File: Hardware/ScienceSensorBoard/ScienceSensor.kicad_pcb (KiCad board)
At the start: 2 copper layers, 96.5 x 94.5 mm, 94 parts, among them J1 Conn_02x03_Counter_Clockwise, J2 RJ45_LED_Shielded, Q1 SI4156DY, Q10 BSS138, Q11 SI4156DY, Q2 SI4156DY, Q3 SI4156DY, Q4 BSS138, Q5 BSS138, Q6 BSS138, Q7 BSS138, Q8 BSS138, Q9 BSS138, U1 TSR_1-2450, U2 OKI-78SR-3.3_1.5-W36H-C, U3 Teensy4.1_DEV-16771, U6 IRS2005S, U7 IRS2005S

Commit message: Layout Reviews Changes
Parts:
- moved V1 0.51 mm to (100.6, 50.8)
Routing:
- net +12V: track 120.9 -> 126.5 mm
- net Micro_FWD: track 63.6 -> 67.0 mm
- net Micro_RVS: track 60.5 -> 63.7 mm
- net +3V3: track 190.7 -> 192.2 mm
- net LED_315: track 49.6 -> 48.2 mm
- net +5V: track 196.6 -> 197.5 mm
- net GND: vias 24 -> 32

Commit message: Molex_SL_06
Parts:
- removed G***: LOGO, MRDT_Silkscreens:0_MRDT_Logo_7.5mm
- Conn4: value Molex_SL_07 -> Molex_SL_06; footprint MRDT_Connectors:MOLEX_SL_07_Horizontal -> UVLEDs:705550040
- moved Conn4 2.54 mm to (108.0, 105.9), turned to -90 degrees
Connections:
- Conn4 pad 4: LED_260 -> LED_275
- Conn4 pad 5: LED_275 -> LED_280
- Conn4 pad 6: LED_280 -> LED_315
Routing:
- net +12V: track 126.5 -> 129.8 mm

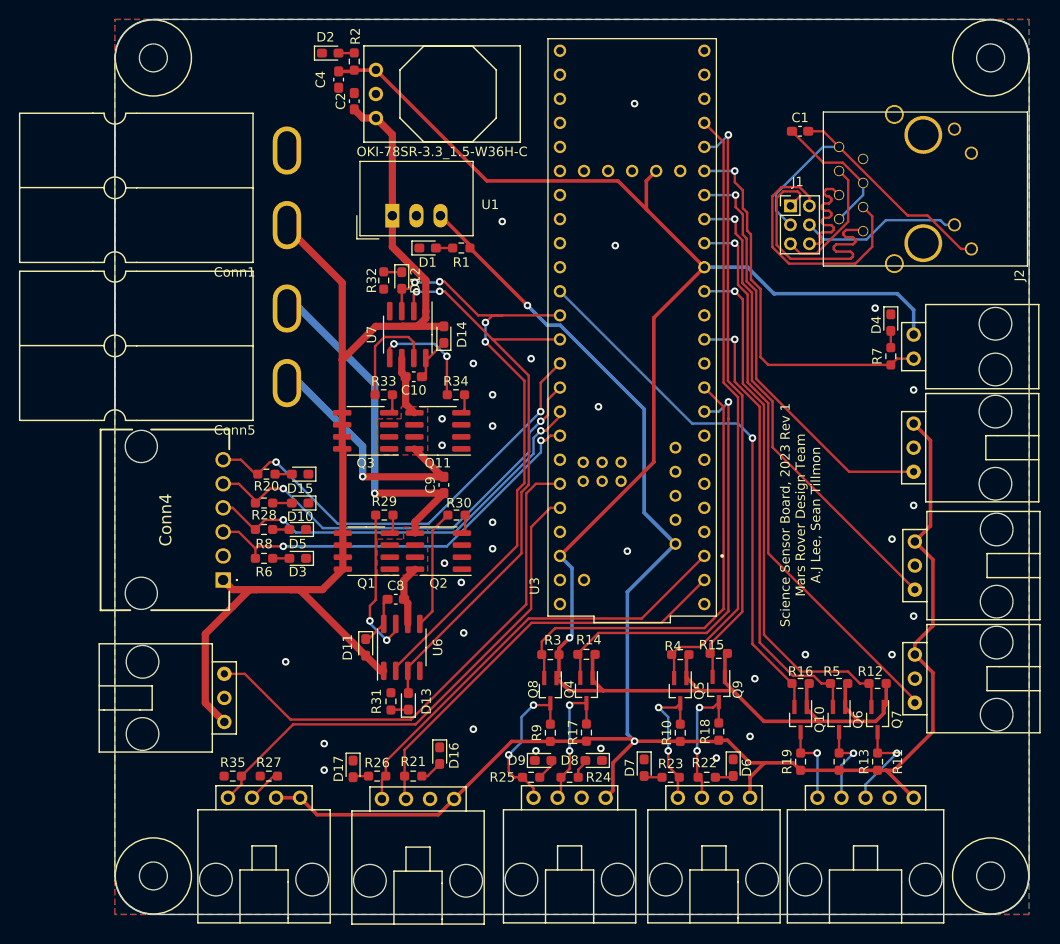
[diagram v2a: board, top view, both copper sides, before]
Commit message: Fixed Schematic error, Labeled some LEDs
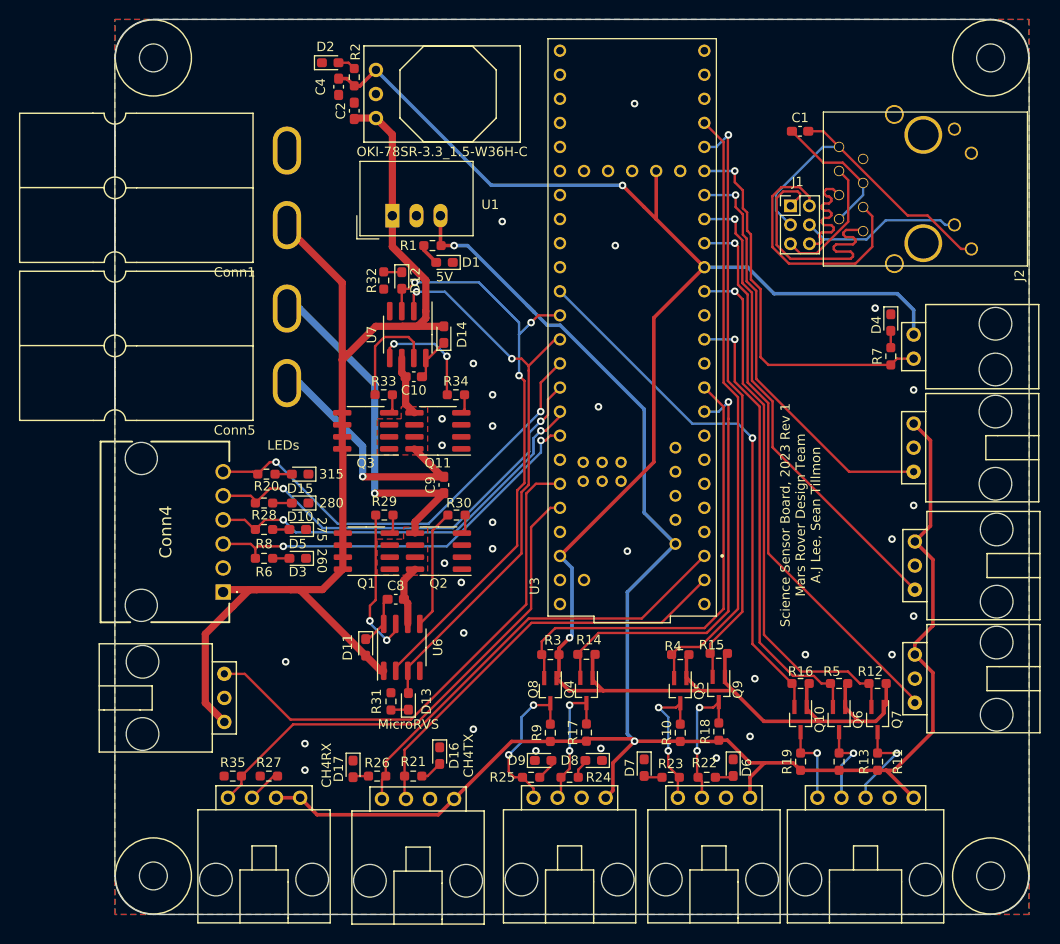
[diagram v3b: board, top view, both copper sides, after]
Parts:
- moved R1 3.06 mm to (130.0, 70.6)
- moved D1 2.34 mm to (131.3, 72.4), turned to 180 degrees
- moved R2 1.65 mm to (121.8, 52.8)
- moved Conn4 1.27 mm to (108.0, 107.2)
- moved C2 1.02 mm to (121.8, 56.4)
- moved D2 1.02 mm to (119.3, 51.3)
- moved C4 0.76 mm to (120.1, 53.8)
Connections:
- Conn4 pad 3: unconnected-(Conn4-Pad3) -> LED_260
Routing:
- net +5V: track 197.5 -> 200.2 mm
- net Micro_FWD: track 67.0 -> 64.6 mm, vias 4 -> 3
- net Micro_RVS: track 63.7 -> 61.6 mm
- net +3V3: track 192.2 -> 193.5 mm, vias 1 -> 2
- net +12V: track 129.8 -> 129.1 mm
- net Net-(D1-Pad2): track 1.77 -> 2.32 mm
- net LED_280: track 47.2 -> 46.7 mm
- net LED_260: track 43.0 -> 42.5 mm
- net LED_315: track 48.2 -> 47.7 mm
- net LED_275: track 44.0 -> 43.5 mm
- net GND: vias 32 -> 31
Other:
- board text added: "260"
- board text added: "275"
- board text added: "280"
- board text added: "315"
- board text added: "5V"
- board text added: "CH4RX"
- board text added: "CH4TX"
- board text added: "MicroRVS"

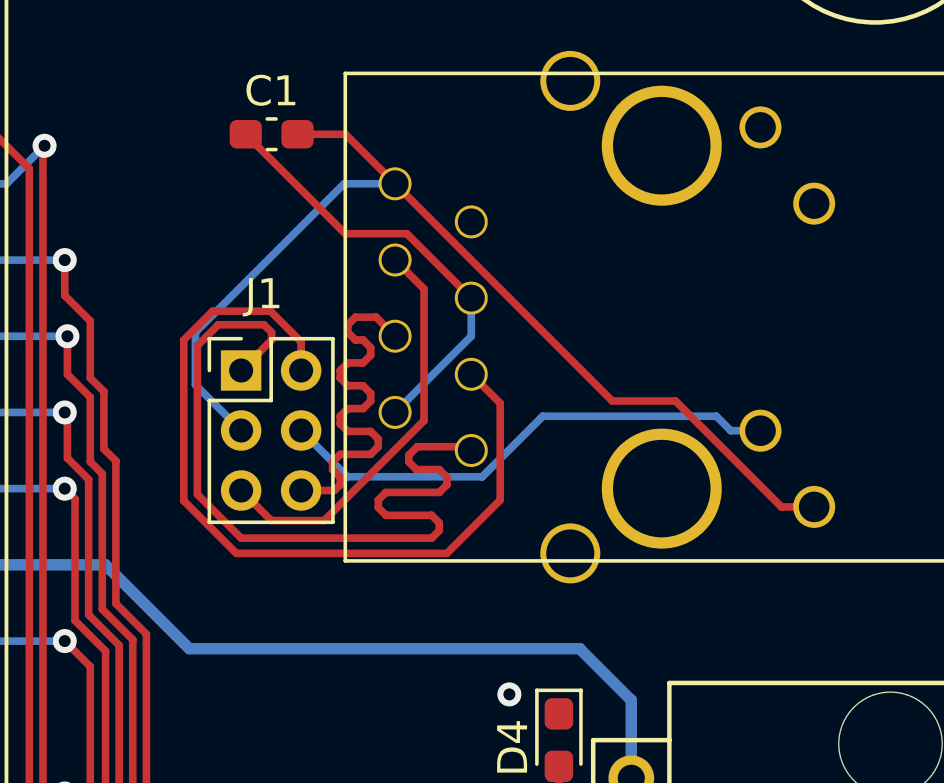
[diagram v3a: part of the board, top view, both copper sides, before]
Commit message: Flipped 2x3, updated sheet boms
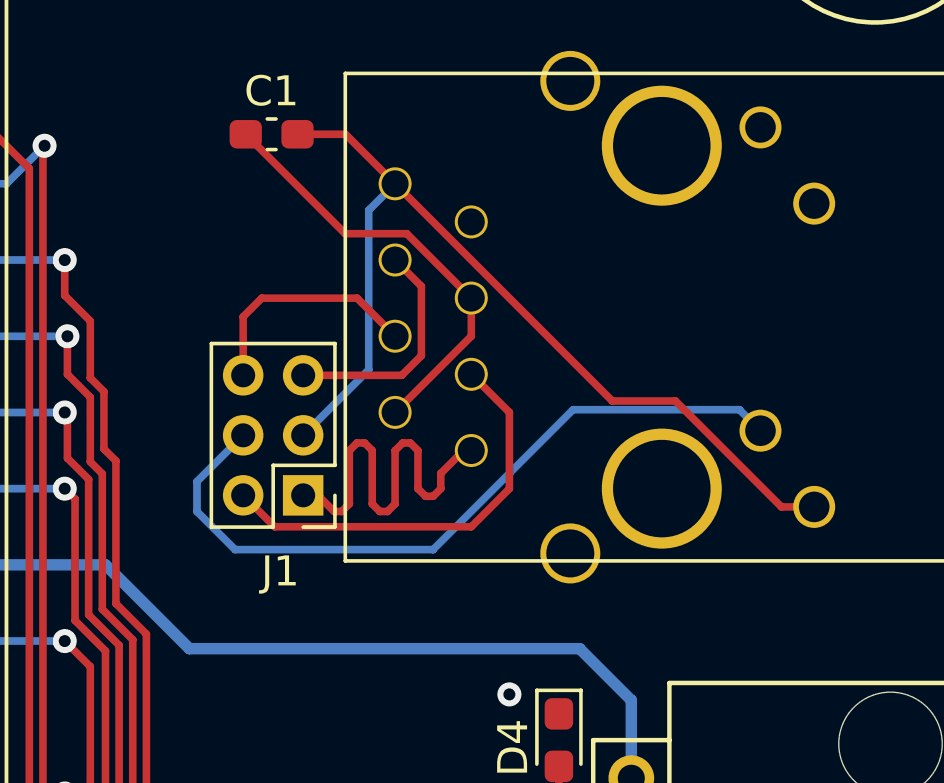
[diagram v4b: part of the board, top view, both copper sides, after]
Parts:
- moved J1 4.65 mm to (169.9, 70.6), turned to 180 degrees
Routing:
- net /Tx+: track 27.7 -> 14.2 mm
- net /Tx-: track 27.6 -> 14.2 mm
- net Net-(J1-Pad4): track 17.0 -> 24.7 mm
- net /Rx-: track 13.6 -> 7.76 mm
- net /Rx+: track 13.6 -> 7.80 mm
- net Net-(C1-Pad2): track 35.0 -> 32.0 mm

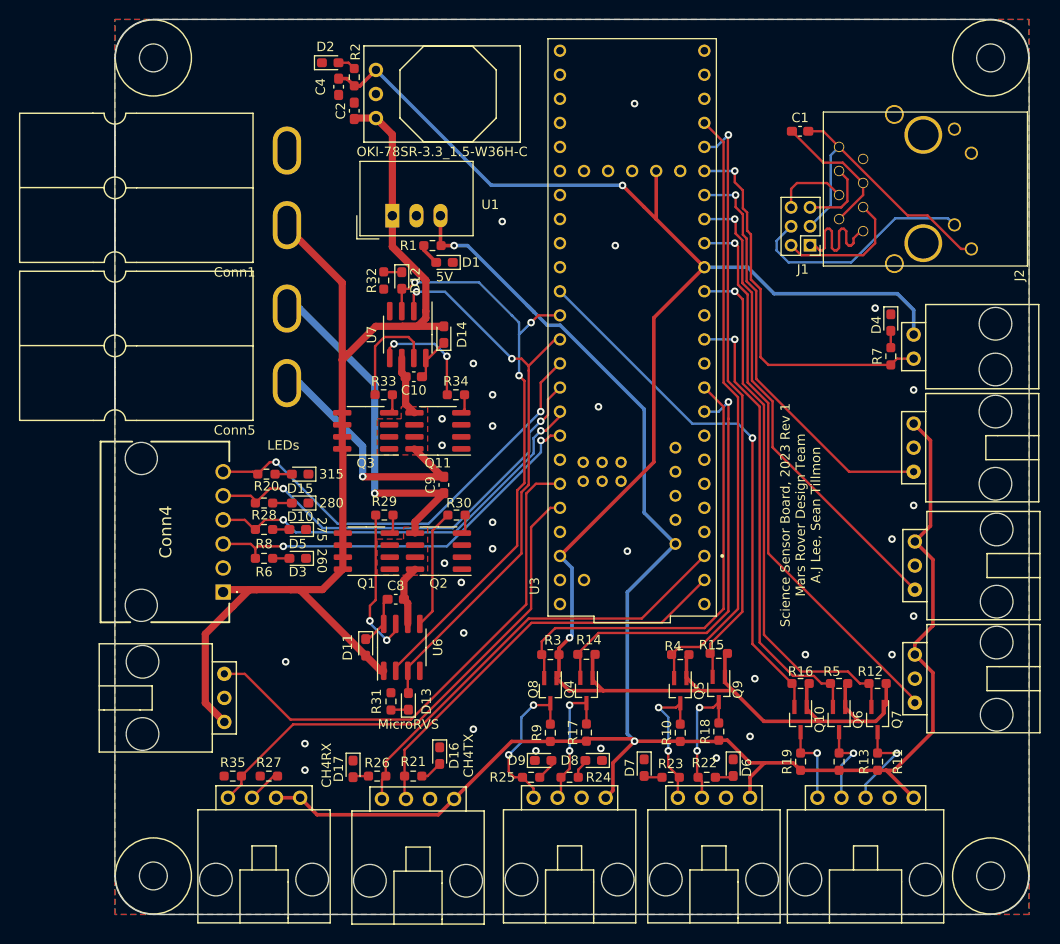
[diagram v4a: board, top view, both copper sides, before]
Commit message: Layout updated for LEDs and Science Sensor Board, schematic for CCD
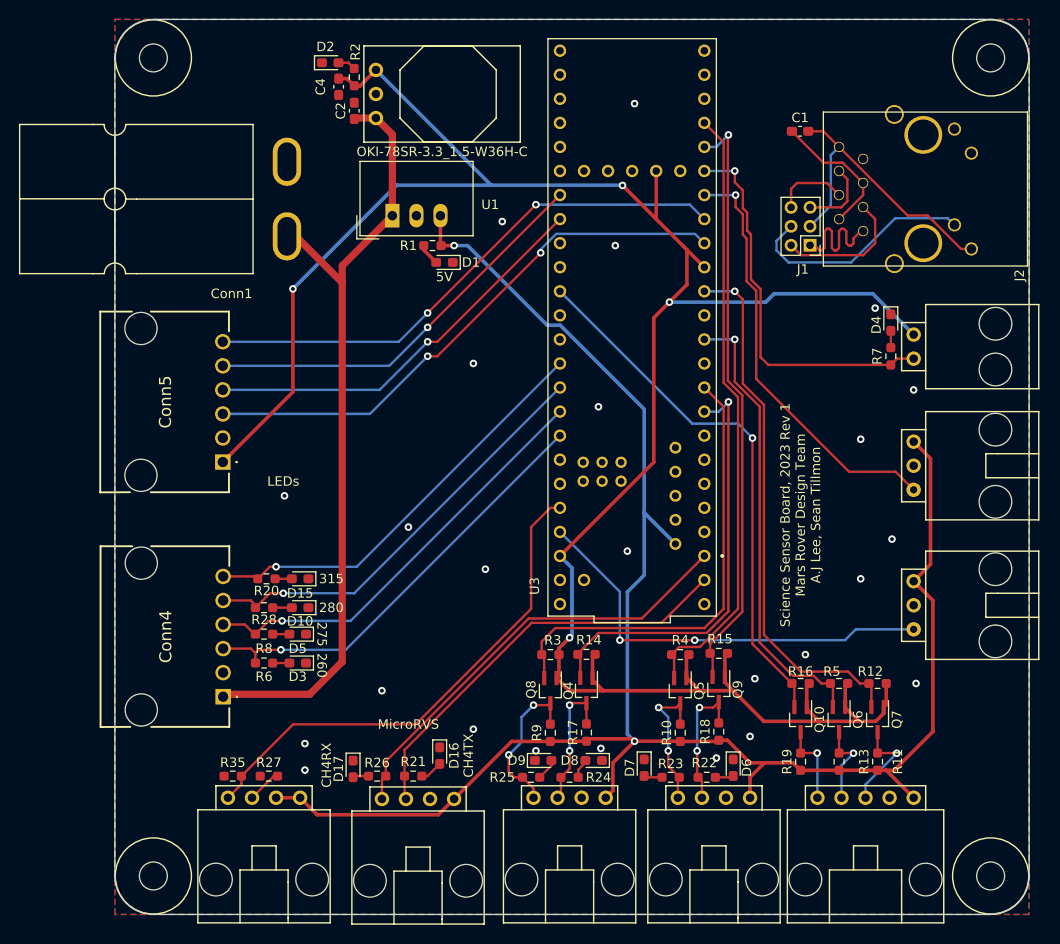
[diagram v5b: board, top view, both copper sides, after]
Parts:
- removed C10, C8: 0.1u, Capacitor_SMD:C_0603_1608Metric_Pad1.08x0.95mm_HandSolder
- removed C9: 10u, Capacitor_SMD:C_0603_1608Metric_Pad1.08x0.95mm_HandSolder
- removed Conn6, Conn7: Molex_SL_03, MRDT_Connectors:MOLEX_SL_03_Horizontal
- removed D11, D14: D_Small, Diode_SMD:D_0603_1608Metric_Pad1.05x0.95mm_HandSolder
- removed D12, D13: Pink, LED_SMD:LED_0603_1608Metric_Pad1.05x0.95mm_HandSolder
- removed Q1, Q11, Q2, Q3: SI4156DY, Package_SO:SOIC-8_3.9x4.9mm_P1.27mm
- removed R29, R30, R33, R34: 100, Resistor_SMD:R_0603_1608Metric_Pad0.98x0.95mm_HandSolder
- removed R31, R32: 120, Resistor_SMD:R_0603_1608Metric_Pad0.98x0.95mm_HandSolder
- removed U6, U7: IRS2005S, Package_SO:SOIC-8_3.9x4.9mm_P1.27mm
- Conn5: value AndersonPP -> Molex_SL_06; footprint MRDT_Connectors:Square_Anderson_2_H_Side_By_Side -> UVLEDs:705550040
- moved Conn5 18.2 mm to (107.9, 93.5), turned to -90 degrees
- moved Conn4 11.0 mm to (108.0, 118.2)
- moved D10 11.0 mm to (116.1, 108.8)
- moved D15 11.0 mm to (116.1, 105.8)
- moved D3 11.0 mm to (115.8, 114.7)
- moved D5 11.0 mm to (115.8, 111.6)
- moved R20 11.0 mm to (112.5, 105.8)
- moved R28 11.0 mm to (112.3, 108.8)
- moved R6 11.0 mm to (112.3, 114.7)
- moved R8 11.0 mm to (112.3, 111.6)
- moved Conn2 4.19 mm to (180.8, 106.0)
- moved Conn12 1.91 mm to (180.8, 91.3)
- moved Conn1 1.18 mm to (115.1, 61.2)
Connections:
- net Micro_Servo renamed Micro_Servo1
- Conn2 pad 3: Photodiode_2 -> Micro_Servo2
- Conn5 pad 1: /M+ -> +3V3
- Conn5 pad 2: /M- -> GND
- U3 pad 14: Micro_FWD -> unconnected-(U3-Pad14)
- U3 pad 15: Micro_RVS -> unconnected-(U3-Pad15)
- U3 pad 21: Micro_ENC -> unconnected-(U3-Pad21)
- U3 pad 23: unconnected-(U3-Pad23) -> Micro_Servo2
- U3 pad 24: Photodiode_1 -> CCD_MC
- U3 pad 25: Photodiode_2 -> CCD_OS
- U3 pad 39: unconnected-(U3-Pad39) -> CCD_ICG
- U3 pad 40: unconnected-(U3-Pad40) -> CCD_SH
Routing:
- net Micro_FWD: track 64.6 -> 0.00 mm, vias 3 -> 0
- net Micro_RVS: track 61.6 -> 0.00 mm, vias 2 -> 0
- net Photodiode_1: track 59.6 -> 0.00 mm, vias 1 -> 0
- net CCD_MC: track 0.00 -> 59.3 mm, vias 0 -> 2
- net CCD_OS: track 0.00 -> 57.5 mm, vias 0 -> 2
- net Micro_ENC: track 54.6 -> 0.00 mm
- net Photodiode_2: track 50.2 -> 0.00 mm, vias 1 -> 0
- net +3V3: track 193.5 -> 243.4 mm, vias 2 -> 4
- net Micro_Servo2: track 0.00 -> 45.5 mm, vias 0 -> 2
- net +12V: track 129.1 -> 84.6 mm
- net /M+: track 43.4 -> 0.00 mm, vias 1 -> 0
- net CCD_SH: track 0.00 -> 43.1 mm, vias 0 -> 1
- net CCD_ICG: track 0.00 -> 43.1 mm, vias 0 -> 1
- net /M-: track 33.2 -> 0.00 mm, vias 1 -> 0
- net Net-(R29-Pad1): track 16.3 -> 0.00 mm, vias 2 -> 0
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- removed copper zone on F.Cu, net /M+
- removed copper zone on F.Cu, net /M-
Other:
- board text added: "+ \ - \MC\SH\ICG\OS"
- board text added: "CCD"
- board text added: "Servo 1"
- board text added: "Servo 2"
- board text removed: "Encoder"
- board text removed: "M+"
- board text removed: "M-"
- board text removed: "Photodiode 1"
- board text removed: "Photodiode 2"
- board text removed: "Servo"

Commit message: Started cleaning up layout
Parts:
- Conn4, Conn5: footprint UVLEDs:705550040 -> Connector_Molex:Molex_SL_171971-0006_1x06_P2.54mm_Vertical
- Q10, Q4, Q5, Q6, Q7, Q8, Q9: footprint Package_TO_SOT_SMD:SOT-323_SC-70_Handsoldering -> Package_TO_SOT_SMD:SOT-23
- moved Conn4 14.3 mm to (102.4, 105.0)
- moved Conn5 13.7 mm to (102.4, 80.9)
- moved D1 10.6 mm to (123.7, 79.8), turned to 0 degrees
- moved R1 9.46 mm to (127.6, 79.8)
- moved U1 9.06 mm to (123.4, 76.2)
- moved C4 6.78 mm to (126.7, 52.3), turned to 180 degrees
- moved R2 5.57 mm to (126.7, 50.3), turned to 0 degrees
- moved C2 4.30 mm to (123.2, 52.3), turned to 0 degrees
- moved D2 4.07 mm to (123.2, 50.3)
- moved U2 2.82 mm to (122.4, 54.9), turned to 0 degrees
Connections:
- J2 pad SH: unconnected-(J2-PadSH) -> GND
- U3 pad VIN: unconnected-(U3-PadVIN) -> +5V
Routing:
- net +3V3: track 243.4 -> 59.3 mm, vias 4 -> 0
- net +5V: track 197.7 -> 27.3 mm, vias 2 -> 0
- net CCD_MC: track 59.3 -> 0.00 mm, vias 2 -> 0
- net Teensy_CO2_RX: track 62.5 -> 3.58 mm, vias 1 -> 0
- net Teensy_CO2_TX: track 64.4 -> 5.91 mm
- net CCD_OS: track 57.5 -> 0.00 mm, vias 2 -> 0
- net Teensy_NO2_SCK: track 57.0 -> 0.37 mm, vias 1 -> 0
- net NH3: track 53.3 -> 2.87 mm
- net Teensy_NO2_MISO: track 56.6 -> 8.09 mm, vias 1 -> 0
- net Teensy_O2_TX: track 48.8 -> 1.74 mm
- net Micro_Servo2: track 45.5 -> 0.00 mm, vias 2 -> 0
- net Micro_Servo1: track 45.1 -> 0.00 mm, vias 1 -> 0
- net Teensy_O2_RX: track 45.5 -> 0.45 mm, vias 1 -> 0
- net Teensy_NO2_CS: track 48.2 -> 4.66 mm, vias 1 -> 0
- net CCD_SH: track 43.1 -> 0.00 mm, vias 1 -> 0
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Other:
- board text added: "3.3V"

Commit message: Finished traces
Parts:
- removed C2: 10 uF, Capacitor_SMD:C_0603_1608Metric_Pad1.08x0.95mm_HandSolder
- removed C4: 10uF, Capacitor_SMD:C_0603_1608Metric_Pad1.08x0.95mm_HandSolder
- removed the U2 at (122.4, 54.9)
- added G***: LOGO, MRDT_Silkscreens:0_MRDT_Logo_10mm, F.Cu at (117.3, 99.6)
- moved D2 12.6 mm to (125.1, 62.7)
- moved R2 12.6 mm to (128.7, 62.7)
- moved R21 12.2 mm to (110.0, 117.7)
- moved D7 12.2 mm to (113.8, 117.7)
- moved R17 6.76 mm to (110.0, 115.2)
- moved D6 6.75 mm to (113.8, 115.2)
- moved R1 6.72 mm to (125.9, 73.3)
- moved U1 6.72 mm to (121.7, 69.7)
- moved D1 6.72 mm to (121.9, 73.3)
- moved R12 5.12 mm to (110.0, 110.1)
- moved D4 5.01 mm to (113.8, 110.1)
- moved D13 3.02 mm to (138.9, 123.8), turned to -90 degrees
- moved R16 2.52 mm to (110.0, 112.6)
- moved D5 2.29 mm to (113.8, 112.6)
- moved D12 2.22 mm to (149.0, 123.8), turned to -90 degrees
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- renumbered Conn9 to Conn10, Conn10 to Conn11, Conn3 to Conn2, Conn2 to Conn3, Conn12 to Conn4, Conn4 to Conn6, Conn11 to Conn7, Conn13 to Conn8, Conn8 to Conn9, D6 to D10, D7 to D11, D8 to D12, D9 to D13, D4 to D3, D3 to D4, D10 to D6, D15 to D7, D16 to D8, D17 to D9, J2 to J1, J1 to J2, Q4 to Q1, Q5 to Q2, Q6 to Q3, Q7 to Q4, Q8 to Q5, Q9 to Q6, Q10 to Q7, R11 to R10, R13 to R11, R6 to R12, R14 to R13, R15 to R14, R16 to R15, R8 to R16, R28 to R17, R17 to R18, R18 to R19, R19 to R20, R20 to R21, R27 to R22, R21 to R23, R26 to R24, R22 to R25, R23 to R26, R24 to R27, R25 to R28, R35 to R29, R7 to R3, R3 to R4, R4 to R5, R5 to R6, R12 to R7, R9 to R8, R10 to R9, U3 to U2
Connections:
- U2 pad 0: CH4_TX -> Teensy_CO2_RX
- U2 pad 1: CH4_RX -> Teensy_CO2_TX
- U2 pad 14: unconnected-(U3-Pad14) -> CH4_RX
- U2 pad 15: unconnected-(U3-Pad15) -> CH4_TX
- U2 pad 16: LED_315 -> CCD_MC
- U2 pad 17: LED_280 -> CCD_OS
- U2 pad 18: LED_275 -> LED_260
- U2 pad 19: LED_260 -> LED_275
- U2 pad 20: unconnected-(U3-Pad20) -> LED_280
- U2 pad 21: unconnected-(U3-Pad21) -> LED_315
- U2 pad 23: Micro_Servo2 -> unconnected-(U2-Pad23)
- U2 pad 24: CCD_MC -> Micro_Servo2
- U2 pad 25: CCD_OS -> Micro_Servo1
- U2 pad 26: Micro_Servo1 -> unconnected-(U2-Pad26)
- U2 pad 28: Teensy_CO2_RX -> unconnected-(U2-Pad28)
- U2 pad 29: Teensy_CO2_TX -> unconnected-(U2-Pad29)
- U2 pad 39: CCD_ICG -> CCD_SH
- U2 pad 40: CCD_SH -> CCD_ICG
- U2 pad USB_GND1: unconnected-(U3-PadUSB_GND1) -> GND
- U2 pad USB_GND2: unconnected-(U3-PadUSB_GND1) -> GND
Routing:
- net +3V3: track 59.3 -> 391.9 mm, vias 0 -> 2
- net +5V: track 27.3 -> 324.2 mm, vias 0 -> 6
- net Teensy_NO2_SCK: track 0.37 -> 63.0 mm, vias 0 -> 1
- net CCD_SH: track 0.00 -> 59.5 mm, vias 0 -> 2
- net Micro_Servo2: track 0.00 -> 58.9 mm
- net CCD_ICG: track 0.00 -> 57.8 mm, vias 0 -> 2
- net CH4_RX: track 4.13 -> 58.8 mm, vias 0 -> 1
- net CH4_TX: track 5.25 -> 55.2 mm, vias 0 -> 1
- net NH3: track 2.87 -> 52.0 mm
- net Micro_Servo1: track 0.00 -> 46.4 mm
- net CCD_OS: track 0.00 -> 44.5 mm
- net Teensy_NO2_MISO: track 8.09 -> 52.0 mm, vias 0 -> 1
- net Teensy_NO2_CS: track 4.66 -> 47.8 mm, vias 0 -> 1
- net CCD_MC: track 0.00 -> 42.4 mm
- net Teensy_O2_TX: track 1.74 -> 41.7 mm, vias 0 -> 1
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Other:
- board text added: "Science Sensor Board, 2023 Rev 1 Mars Rover Design Team A.J Lee, Sean Tillmon,Grant Brinker"
- board text removed: "Science Sensor Board, 2023 Rev 1 Mars Rover Design Team A.J Lee, Sean Tillmon"
